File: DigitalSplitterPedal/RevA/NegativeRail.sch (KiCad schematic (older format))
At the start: 3 parts, among them U3 TPS60400

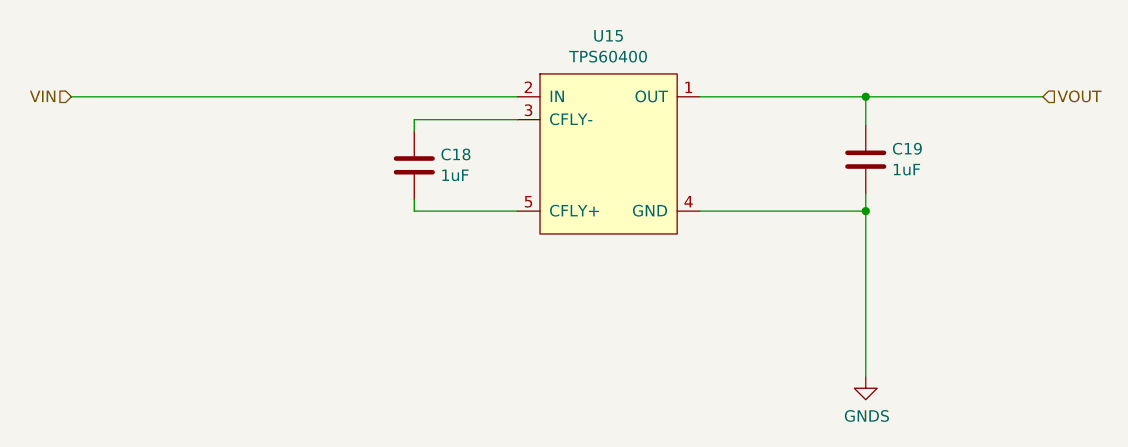
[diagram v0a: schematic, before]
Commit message: HW update
- Completed RevA layout (draft)
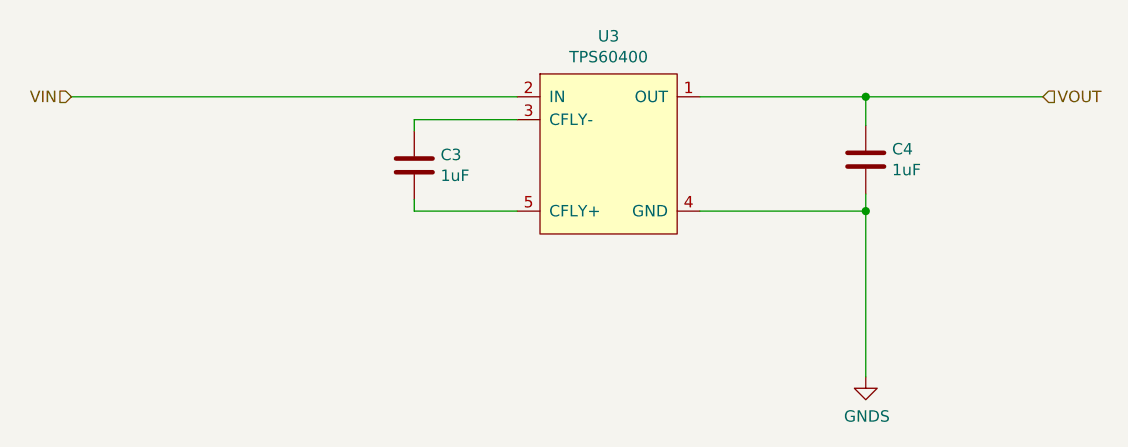
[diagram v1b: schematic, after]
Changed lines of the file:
@@
 AR Path="/5F6F456E/5F6CB881" Ref="U14"  Part="1"
 AR Path="/5F6F8B66/5F6CB881" Ref="U15"  Part="1"
-F 0 "U15" H 5300 3915 50  0000 C CNN
+F 0 "U3" H 5300 3915 50  0000 C CNN
 F 1 "TPS60400" H 5300 3824 50  0000 C CNN
 F 2 "Package_TO_SOT_SMD:SOT-23-5_HandSoldering" H 5300 3823 50  0001 C CNN
@@
 AR Path="/5F6F456E/5F6CBB44" Ref="C7"  Part="1"
 AR Path="/5F6F8B66/5F6CBB44" Ref="C18"  Part="1"
-F 0 "C18" H 4565 3496 50  0000 L CNN
+F 0 "C3" H 4565 3496 50  0000 L CNN
 F 1 "1uF" H 4565 3405 50  0000 L CNN
 F 2 "Capacitor_SMD:C_0805_2012Metric_Pad1.15x1.40mm_HandSolder" H 4488 3300 50  0001 C CNN
@@
 AR Path="/5F6F456E/5F6CC1BA" Ref="#PWR0150"  Part="1"
 AR Path="/5F6F8B66/5F6CC1BA" Ref="#PWR0157"  Part="1"
-F 0 "#PWR0157" H 6425 4125 50  0001 C CNN
+F 0 "#PWR0110" H 6425 4125 50  0001 C CNN
 F 1 "GNDS" H 6430 4202 50  0000 C CNN
 F 2 "" H 6425 4375 50  0001 C CNN
@@
 AR Path="/5F6F456E/5F6CC20E" Ref="C11"  Part="1"
 AR Path="/5F6F8B66/5F6CC20E" Ref="C19"  Part="1"
-F 0 "C19" H 6540 3471 50  0000 L CNN
+F 0 "C4" H 6540 3471 50  0000 L CNN
 F 1 "1uF" H 6540 3380 50  0000 L CNN
 F 2 "Capacitor_SMD:C_0805_2012Metric_Pad1.15x1.40mm_HandSolder" H 6463 3275 50  0001 C CNN

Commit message: updated hw
- add testpoints
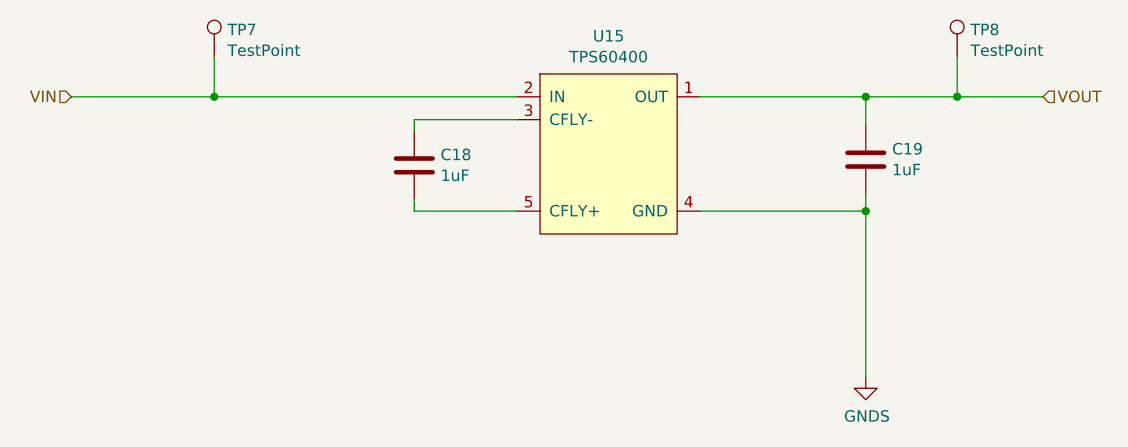
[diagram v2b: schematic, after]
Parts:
- added TP1, TP2: TestPoint, TestPoint:TestPoint_Pad_D1.0mm, symbol Connector:TestPoint
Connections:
- net VIN: now also TP1.1
- net VOUT: now also TP2.1
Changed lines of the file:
@@
 $Descr A4 11693 8268
 encoding utf-8
-Sheet 6 15
+Sheet 12 15
 Title ""
 Date ""
@@
 AR Path="/5F6F456E/5F6CB881" Ref="U14"  Part="1"
 AR Path="/5F6F8B66/5F6CB881" Ref="U15"  Part="1"
-F 0 "U3" H 5300 3915 50  0000 C CNN
+F 0 "U15" H 5300 3915 50  0000 C CNN
 F 1 "TPS60400" H 5300 3824 50  0000 C CNN
 F 2 "Package_TO_SOT_SMD:SOT-23-5_HandSoldering" H 5300 3823 50  0001 C CNN
@@
 AR Path="/5F6F456E/5F6CBB44" Ref="C7"  Part="1"
 AR Path="/5F6F8B66/5F6CBB44" Ref="C18"  Part="1"
-F 0 "C3" H 4565 3496 50  0000 L CNN
+F 0 "C18" H 4565 3496 50  0000 L CNN
 F 1 "1uF" H 4565 3405 50  0000 L CNN
 F 2 "Capacitor_SMD:C_0805_2012Metric_Pad1.15x1.40mm_HandSolder" H 4488 3300 50  0001 C CNN
@@
 	4450 3650 4900 3650
 Wire Wire Line
-	4900 3150 2950 3150
+	4900 3150 3575 3150
 Text HLabel 2950 3150 0    50   Input ~ 0
 VIN
@@
 AR Path="/5F6F456E/5F6CC1BA" Ref="#PWR0150"  Part="1"
 AR Path="/5F6F8B66/5F6CC1BA" Ref="#PWR0157"  Part="1"
-F 0 "#PWR0110" H 6425 4125 50  0001 C CNN
+F 0 "#PWR0157" H 6425 4125 50  0001 C CNN
 F 1 "GNDS" H 6430 4202 50  0000 C CNN
 F 2 "" H 6425 4375 50  0001 C CNN
@@
 AR Path="/5F6F456E/5F6CC20E" Ref="C11"  Part="1"
 AR Path="/5F6F8B66/5F6CC20E" Ref="C19"  Part="1"
-F 0 "C4" H 6540 3471 50  0000 L CNN
+F 0 "C19" H 6540 3471 50  0000 L CNN
 F 1 "1uF" H 6540 3380 50  0000 L CNN
 F 2 "Capacitor_SMD:C_0805_2012Metric_Pad1.15x1.40mm_HandSolder" H 6463 3275 50  0001 C CNN
@@
 Connection ~ 6425 3150
 Wire Wire Line
-	6425 3150 7200 3150
+	6425 3150 6825 3150
 Wire Wire Line
 	6425 3575 6425 3650
 Connection ~ 6425 3650
+$Comp
+L Connector:TestPoint TP1
+U 1 1 5F6DE647
+P 3575 2975
+AR Path="/5F6CB11D/5F6DE647" Ref="TP1"  Part="1"
+AR Path="/5F6F05C2/5F6DE647" Ref="TP3"  Part="1"
+AR Path="/5F6F456E/5F6DE647" Ref="TP5"  Part="1"
+AR Path="/5F6F8B66/5F6DE647" Ref="TP7"  Part="1"
+F 0 "TP7" H 3633 3093 50  0000 L CNN
+F 1 "TestPoint" H 3633 3002 50  0000 L CNN
+F 2 "TestPoint:TestPoint_Pad_D1.0mm" H 3775 2975 50  0001 C CNN
+F 3 "~" H 3775 2975 50  0001 C CNN
+	1    3575 2975
+	1    0    0    -1
+$EndComp
+Wire Wire Line
+	3575 2975 3575 3150
+Connection ~ 3575 3150
+Wire Wire Line
+	3575 3150 2950 3150
+$Comp
+L Connector:TestPoint TP2
+U 1 1 5F6DF27F
+P 6825 2975
+AR Path="/5F6CB11D/5F6DF27F" Ref="TP2"  Part="1"
+AR Path="/5F6F05C2/5F6DF27F" Ref="TP4"  Part="1"
+AR Path="/5F6F456E/5F6DF27F" Ref="TP6"  Part="1"
+AR Path="/5F6F8B66/5F6DF27F" Ref="TP8"  Part="1"
+F 0 "TP8" H 6883 3093 50  0000 L CNN
+F 1 "TestPoint" H 6883 3002 50  0000 L CNN
+F 2 "TestPoint:TestPoint_Pad_D1.0mm" H 7025 2975 50  0001 C CNN
+F 3 "~" H 7025 2975 50  0001 C CNN
+	1    6825 2975
+	1    0    0    -1
+$EndComp
+Wire Wire Line
+	6825 2975 6825 3150
+Connection ~ 6825 3150
+Wire Wire Line
+	6825 3150 7200 3150
 $EndSCHEMATC
